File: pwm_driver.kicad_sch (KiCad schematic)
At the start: 148 parts, among them J11 POWER, Q1 Si7450DP, Q10 Si7450DP, Q11 Si7450DP, Q12 Si7450DP, Q13 Si7450DP, Q14 Si7450DP, Q15 Si7450DP, Q16 Si7450DP, Q2 Si7450DP, Q3 Si7450DP, Q4 Si7450DP, Q5 Si7450DP, Q6 Si7450DP, Q7 Si7450DP, Q8 Si7450DP, Q9 Si7450DP

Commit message: Replaced 0603 Caps (VPP) with 1206
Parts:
- C23, C24, C25, C26, C27, C28, C29, C30, C31, C32, C33, C34, C55, C56, C57, C58, C59, C60, C61, C62, C63, C64, C65, C66: footprint Capacitor_SMD:C_0603_1608Metric -> SeniorDesign:C_1206_3216Metric
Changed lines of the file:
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@@
       (effects (font (size 1.27 1.27)) (justify left))
     )
-    (property "Footprint" "Capacitor_SMD:C_0603_1608Metric" (id 2) (at 169.8752 76.2 0)
+    (property "Footprint" "SeniorDesign:C_1206_3216Metric" (id 2) (at 169.8752 76.2 0)
       (effects (font (size 1.27 1.27)) hide)
     )
@@
       (effects (font (size 1.27 1.27)) (justify right))
     )
-    (property "Footprint" "Capacitor_SMD:C_0603_1608Metric" (id 2) (at 176.8348 68.58 0)
+    (property "Footprint" "SeniorDesign:C_1206_3216Metric" (id 2) (at 176.8348 68.58 0)
       (effects (font (size 1.27 1.27)) hide)
     )
@@
       (effects (font (size 1.27 1.27)) (justify right))
     )
-    (property "Footprint" "Capacitor_SMD:C_0603_1608Metric" (id 2) (at 186.9948 68.58 0)
+    (property "Footprint" "SeniorDesign:C_1206_3216Metric" (id 2) (at 186.9948 68.58 0)
       (effects (font (size 1.27 1.27)) hide)
     )
@@
       (effects (font (size 1.27 1.27)) (justify left))
     )
-    (property "Footprint" "Capacitor_SMD:C_0603_1608Metric" (id 2) (at 169.8752 111.76 0)
+    (property "Footprint" "SeniorDesign:C_1206_3216Metric" (id 2) (at 169.8752 111.76 0)
       (effects (font (size 1.27 1.27)) hide)
     )
@@
       (effects (font (size 1.27 1.27)) (justify right))
     )
-    (property "Footprint" "Capacitor_SMD:C_0603_1608Metric" (id 2) (at 176.8348 104.14 0)
+    (property "Footprint" "SeniorDesign:C_1206_3216Metric" (id 2) (at 176.8348 104.14 0)
       (effects (font (size 1.27 1.27)) hide)
     )
@@
       (effects (font (size 1.27 1.27)) (justify right))
     )
-    (property "Footprint" "Capacitor_SMD:C_0603_1608Metric" (id 2) (at 186.9948 104.14 0)
+    (property "Footprint" "SeniorDesign:C_1206_3216Metric" (id 2) (at 186.9948 104.14 0)
       (effects (font (size 1.27 1.27)) hide)
     )
@@
       (effects (font (size 1.27 1.27)) (justify left))
     )
-    (property "Footprint" "Capacitor_SMD:C_0603_1608Metric" (id 2) (at 169.8752 147.32 0)
+    (property "Footprint" "SeniorDesign:C_1206_3216Metric" (id 2) (at 169.8752 147.32 0)
       (effects (font (size 1.27 1.27)) hide)
     )
@@
       (effects (font (size 1.27 1.27)) (justify right))
     )
-    (property "Footprint" "Capacitor_SMD:C_0603_1608Metric" (id 2) (at 176.8348 139.7 0)
+    (property "Footprint" "SeniorDesign:C_1206_3216Metric" (id 2) (at 176.8348 139.7 0)
       (effects (font (size 1.27 1.27)) hide)
     )
@@
       (effects (font (size 1.27 1.27)) (justify right))
     )
-    (property "Footprint" "Capacitor_SMD:C_0603_1608Metric" (id 2) (at 186.9948 139.7 0)
+    (property "Footprint" "SeniorDesign:C_1206_3216Metric" (id 2) (at 186.9948 139.7 0)
       (effects (font (size 1.27 1.27)) hide)
     )
@@
       (effects (font (size 1.27 1.27)) (justify left))
     )
-    (property "Footprint" "Capacitor_SMD:C_0603_1608Metric" (id 2) (at 169.8752 182.88 0)
+    (property "Footprint" "SeniorDesign:C_1206_3216Metric" (id 2) (at 169.8752 182.88 0)
       (effects (font (size 1.27 1.27)) hide)
     )
@@
       (effects (font (size 1.27 1.27)) (justify right))
     )
-    (property "Footprint" "Capacitor_SMD:C_0603_1608Metric" (id 2) (at 176.8348 175.26 0)
+    (property "Footprint" "SeniorDesign:C_1206_3216Metric" (id 2) (at 176.8348 175.26 0)
       (effects (font (size 1.27 1.27)) hide)
     )
@@
       (effects (font (size 1.27 1.27)) (justify right))
     )
-    (property "Footprint" "Capacitor_SMD:C_0603_1608Metric" (id 2) (at 186.9948 175.26 0)
+    (property "Footprint" "SeniorDesign:C_1206_3216Metric" (id 2) (at 186.9948 175.26 0)
       (effects (font (size 1.27 1.27)) hide)
     )
@@
       (effects (font (size 1.27 1.27)) (justify left))
     )
-    (property "Footprint" "Capacitor_SMD:C_0603_1608Metric" (id 2) (at 340.0552 76.2 0)
+    (property "Footprint" "SeniorDesign:C_1206_3216Metric" (id 2) (at 340.0552 76.2 0)
       (effects (font (size 1.27 1.27)) hide)
     )
@@
       (effects (font (size 1.27 1.27)) (justify right))
     )
-    (property "Footprint" "Capacitor_SMD:C_0603_1608Metric" (id 2) (at 347.0148 68.58 0)
+    (property "Footprint" "SeniorDesign:C_1206_3216Metric" (id 2) (at 347.0148 68.58 0)
       (effects (font (size 1.27 1.27)) hide)
     )
@@
       (effects (font (size 1.27 1.27)) (justify right))
     )
-    (property "Footprint" "Capacitor_SMD:C_0603_1608Metric" (id 2) (at 357.1748 68.58 0)
+    (property "Footprint" "SeniorDesign:C_1206_3216Metric" (id 2) (at 357.1748 68.58 0)
       (effects (font (size 1.27 1.27)) hide)
     )
@@
       (effects (font (size 1.27 1.27)) (justify left))
     )
-    (property "Footprint" "Capacitor_SMD:C_0603_1608Metric" (id 2) (at 340.0552 111.76 0)
+    (property "Footprint" "SeniorDesign:C_1206_3216Metric" (id 2) (at 340.0552 111.76 0)
       (effects (font (size 1.27 1.27)) hide)
     )
@@
       (effects (font (size 1.27 1.27)) (justify right))
     )
-    (property "Footprint" "Capacitor_SMD:C_0603_1608Metric" (id 2) (at 347.0148 104.14 0)
+    (property "Footprint" "SeniorDesign:C_1206_3216Metric" (id 2) (at 347.0148 104.14 0)
       (effects (font (size 1.27 1.27)) hide)
     )
@@
       (effects (font (size 1.27 1.27)) (justify right))
     )
-    (property "Footprint" "Capacitor_SMD:C_0603_1608Metric" (id 2) (at 357.1748 104.14 0)
+    (property "Footprint" "SeniorDesign:C_1206_3216Metric" (id 2) (at 357.1748 104.14 0)
       (effects (font (size 1.27 1.27)) hide)
     )
@@
       (effects (font (size 1.27 1.27)) (justify left))
     )
-    (property "Footprint" "Capacitor_SMD:C_0603_1608Metric" (id 2) (at 340.0552 147.32 0)
+    (property "Footprint" "SeniorDesign:C_1206_3216Metric" (id 2) (at 340.0552 147.32 0)
       (effects (font (size 1.27 1.27)) hide)
     )
@@
       (effects (font (size 1.27 1.27)) (justify right))
     )
-    (property "Footprint" "Capacitor_SMD:C_0603_1608Metric" (id 2) (at 347.0148 139.7 0)
+    (property "Footprint" "SeniorDesign:C_1206_3216Metric" (id 2) (at 347.0148 139.7 0)
       (effects (font (size 1.27 1.27)) hide)
     )
@@
       (effects (font (size 1.27 1.27)) (justify right))
     )
-    (property "Footprint" "Capacitor_SMD:C_0603_1608Metric" (id 2) (at 357.1748 139.7 0)
+    (property "Footprint" "SeniorDesign:C_1206_3216Metric" (id 2) (at 357.1748 139.7 0)
       (effects (font (size 1.27 1.27)) hide)
     )
@@
       (effects (font (size 1.27 1.27)) (justify left))
     )
-    (property "Footprint" "Capacitor_SMD:C_0603_1608Metric" (id 2) (at 340.0552 182.88 0)
+    (property "Footprint" "SeniorDesign:C_1206_3216Metric" (id 2) (at 340.0552 182.88 0)
       (effects (font (size 1.27 1.27)) hide)
     )
@@
       (effects (font (size 1.27 1.27)) (justify right))
     )
-    (property "Footprint" "Capacitor_SMD:C_0603_1608Metric" (id 2) (at 347.0148 175.26 0)
+    (property "Footprint" "SeniorDesign:C_1206_3216Metric" (id 2) (at 347.0148 175.26 0)
       (effects (font (size 1.27 1.27)) hide)
     )
@@
       (effects (font (size 1.27 1.27)) (justify right))
     )
-    (property "Footprint" "Capacitor_SMD:C_0603_1608Metric" (id 2) (at 357.1748 175.26 0)
-      (effects (font (size 1.27 1.27)) hide)
-    )
+    (property "Footprint" "SeniorDesign:C_1206_3216Metric" (id 2) (at 357.1748 175.26 0)
+      (effects (font (size 1.27 1.27)) hide)
+    )

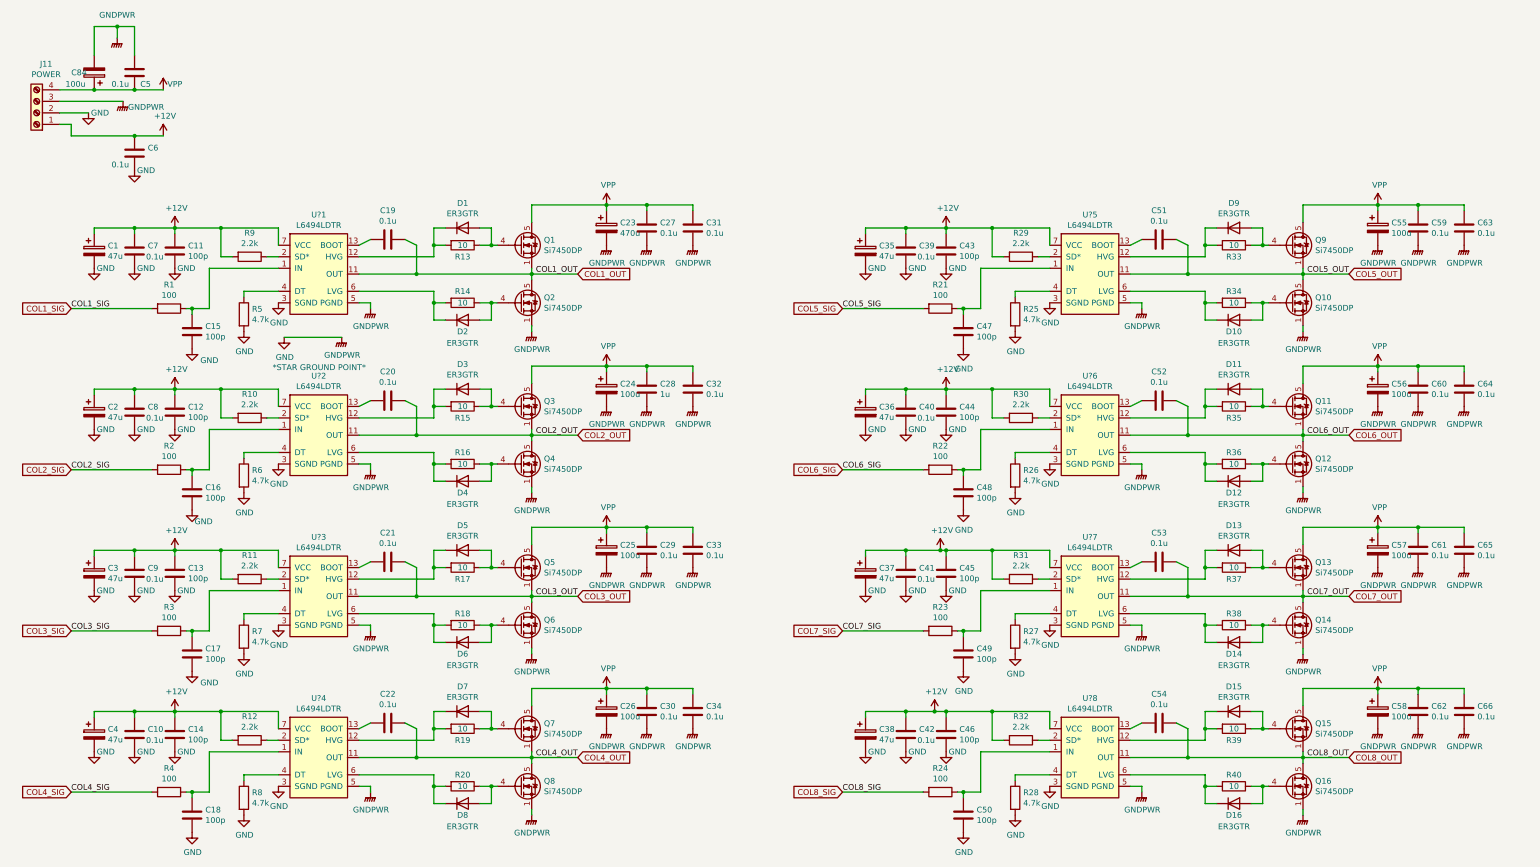
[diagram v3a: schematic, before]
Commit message: final pre-design review push
Fixed some routing problems. Changed capacitor sizes for large bypass voltages. array modeled
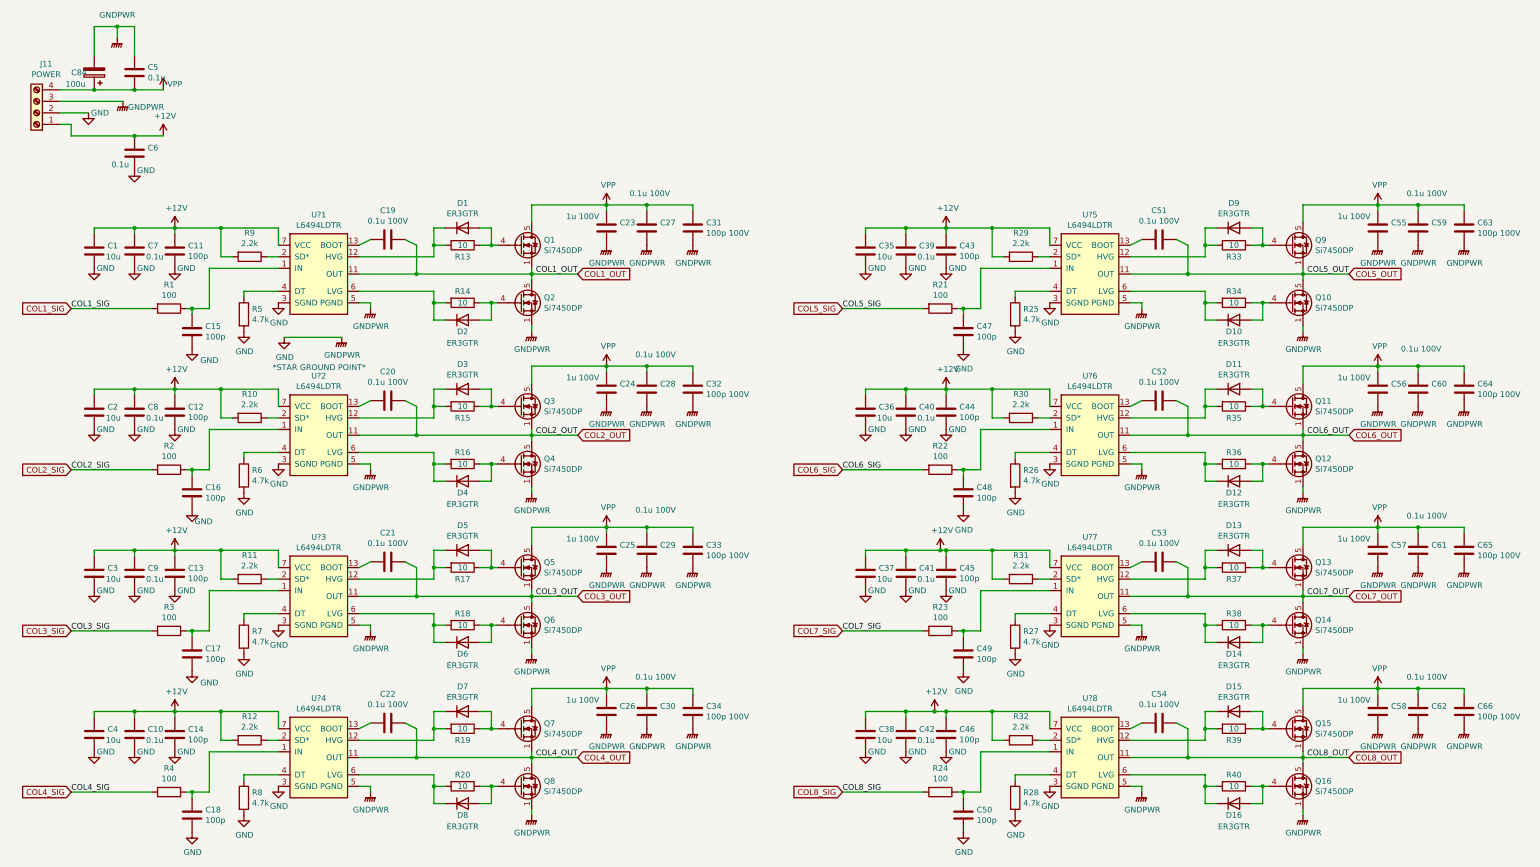
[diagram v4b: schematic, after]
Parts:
- removed C1, C2, C3, C35, C36, C37, C38, C4: 47u, Capacitor_SMD:C_0603_1608Metric, symbol Device:CP
- removed C23: 470u, SeniorDesign:C_1206_3216Metric, symbol Device:CP
- removed C24, C25, C26, C55, C56, C57, C58: 100u, SeniorDesign:C_1206_3216Metric, symbol Device:CP
- added C1, C2, C3, C35, C36, C37, C38, C4: 10u, Capacitor_SMD:C_0603_1608Metric, symbol Device:C
- added C23, C24, C25, C26, C55, C56, C57, C58: 1u 100V, SeniorDesign:C_1206_3216Metric, symbol Device:C
- C19, C20, C21, C22, C51, C52, C53, C54: value 0.1u -> 0.1u 100V; footprint Capacitor_SMD:C_0603_1608Metric -> Capacitor_SMD:C_0805_2012Metric
- C27, C29, C30, C59, C60, C61, C62: value 0.1u -> 0.1u 100V
- C28: value 1u -> 0.1u 100V
- C31, C32, C33, C34, C63, C64, C65, C66: value 0.1u -> 100p 100V
- C5: footprint Capacitor_SMD:C_0603_1608Metric -> SeniorDesign:C_1206_3216Metric
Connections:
- net +12V: now also C1.2, C2.2, C3.2, C35.2, C36.2, C37.2, C38.2, C4.2
- net GND: now also C5.2, C1.1, C2.1, C23.1, C24.1, C25.1, C26.1, C3.1, C35.1, C36.1, C37.1, C38.1, C4.1, C55.1, C56.1, C57.1, C58.1; no longer C5.1
- net VPP: now also C5.1, C23.2, C24.2, C25.2, C26.2, C55.2, C56.2, C57.2, C58.2; no longer C5.2
